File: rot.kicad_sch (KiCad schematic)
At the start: 35 parts, among them J4 PinSocket_2x6_P2.54mm_Drill1.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, J8 Plug_Molex_SlimStack_2x25_529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, U2 W25Q32JW_SOIC-8, U3 W25Q32JW_SOIC-8, U4 W25Q32JW_SOIC-8, U5 W25Q32JW_SOIC-8

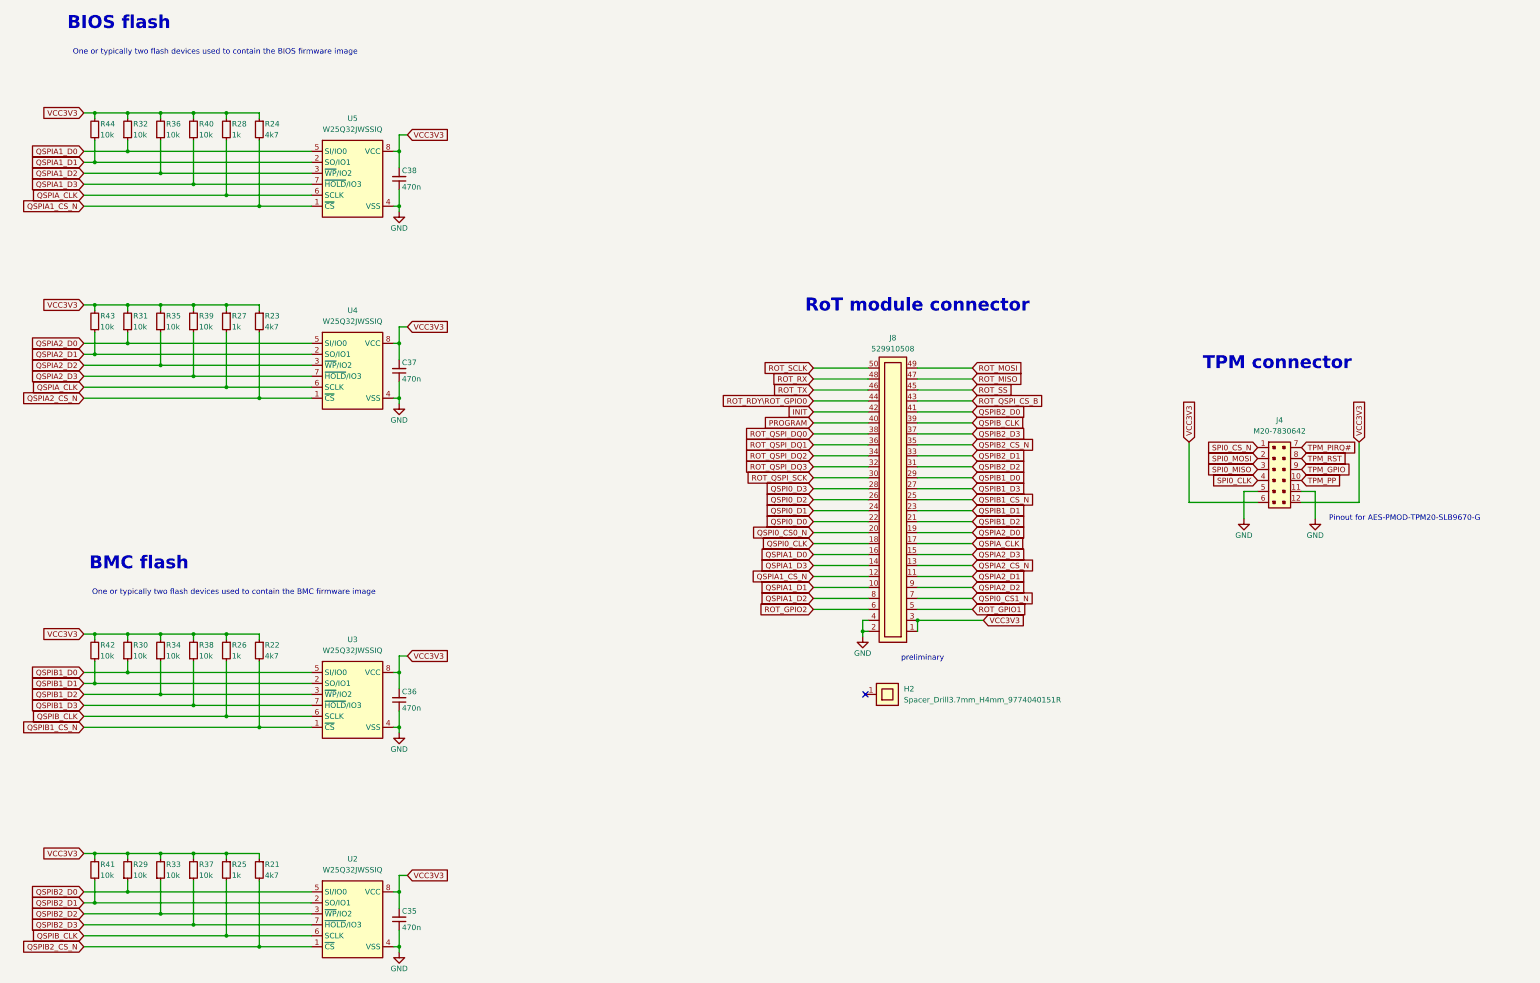
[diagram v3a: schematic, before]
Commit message: [#68236] Allign sch to grid
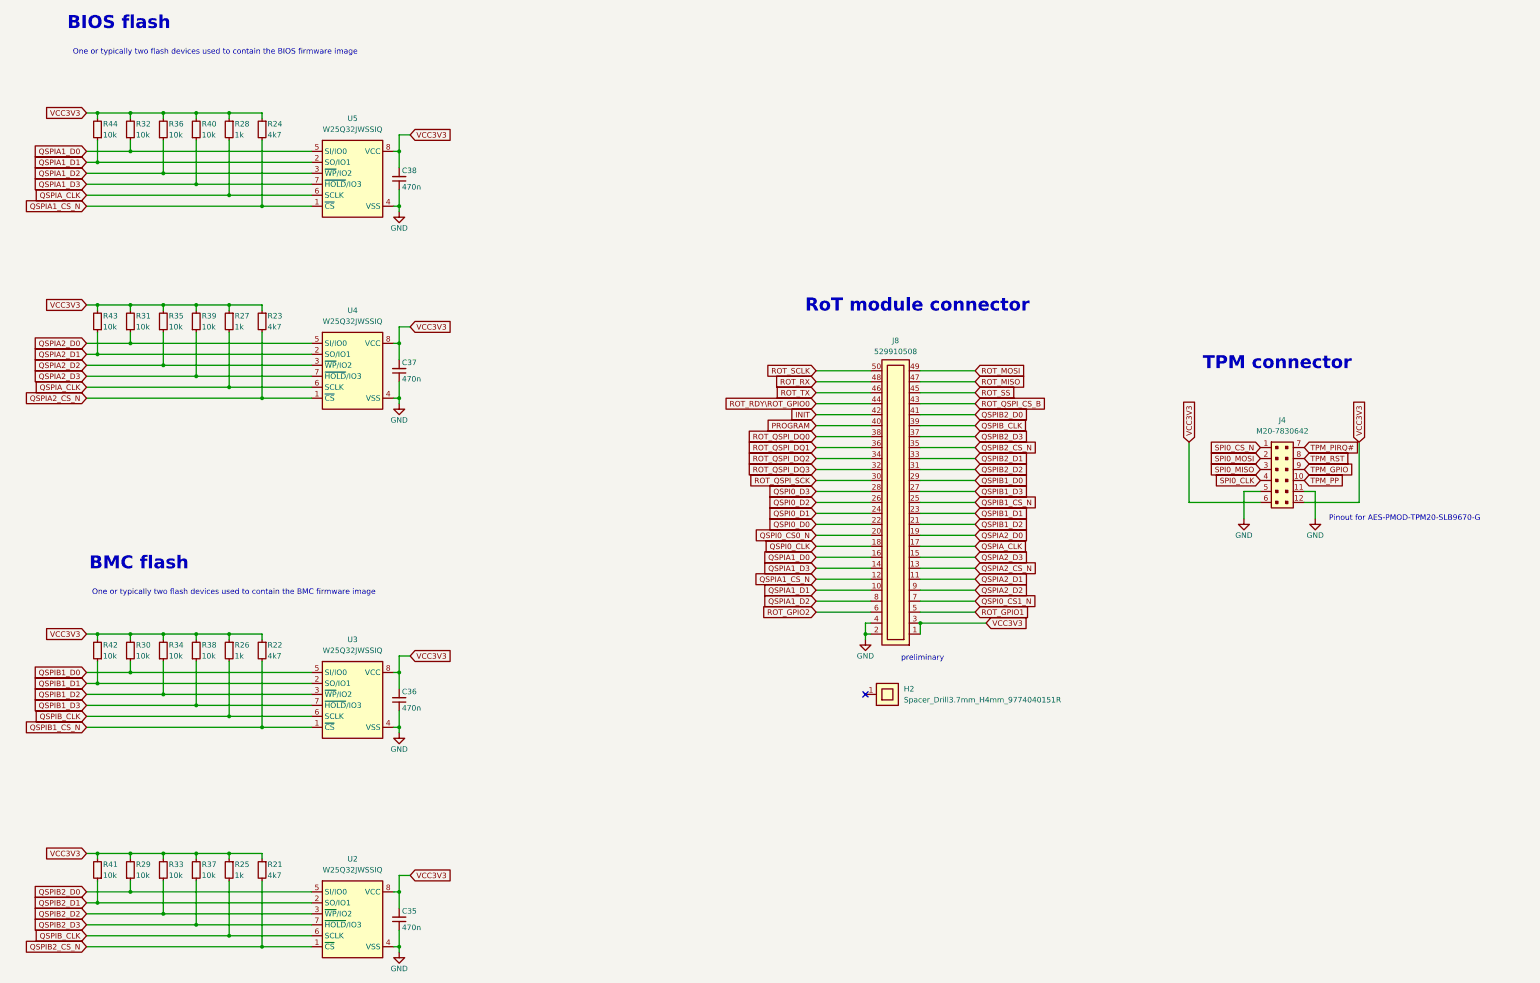
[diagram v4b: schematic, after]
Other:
- moved on the sheet: J4, J8, R21, R22, R23, R24, R25, R26, R27, R28, R29, R30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
